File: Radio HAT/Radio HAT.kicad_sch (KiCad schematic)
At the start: 15 parts, among them J1 Raspberry_Pi_2_3, J2 Coax SMA, J3 Barrel_Jack, U1 RFM98PW, U2 AZ2185D-ADJTRG1

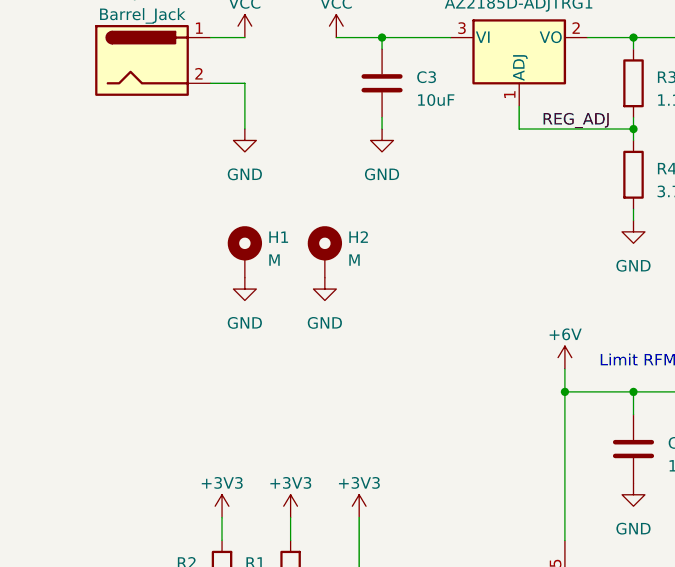
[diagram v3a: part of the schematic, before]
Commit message: Implemented changes from PR
Fixed 3D models of board, added testpoints on board.
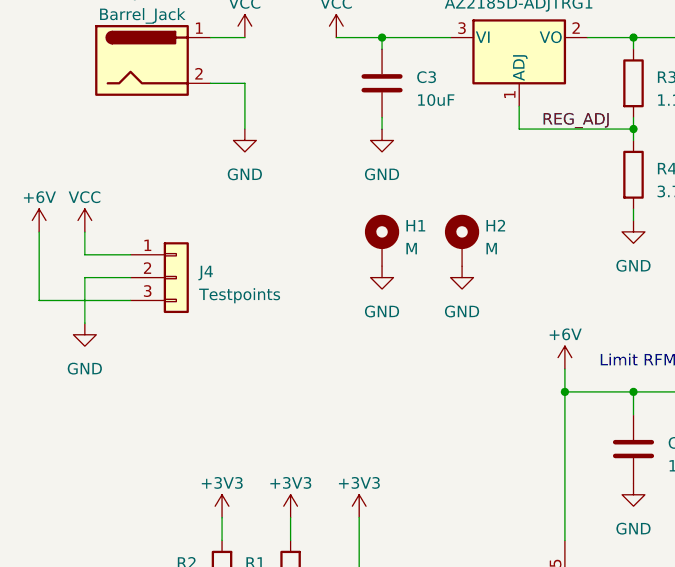
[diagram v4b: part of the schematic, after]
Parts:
- added J4: Testpoints, Connector_PinSocket_2.54mm:PinSocket_1x03_P2.54mm_Vertical, symbol Connector_Generic:Conn_01x03
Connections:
- net +6V: now also J4.3 (Pin_3)
- net GND: now also J4.2 (Pin_2)
- net VCC: now also J4.1 (Pin_1)
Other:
- moved on the sheet: H1, H2
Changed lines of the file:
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@@
+    (stroke (width 0) (type default))
+  )
+  (wire (pts (xy 50.8 80.01) (xy 40.64 80.01))
     (stroke (width 0) (type default))
   )
@@
     (stroke (width 0) (type default))
   )
+  (wire (pts (xy 45.72 72.39) (xy 45.72 74.93))
+    (stroke (width 0) (type default))
+  )
   (wire (pts (xy 63.5 55.88) (xy 63.5 60.96))
     (stroke (width 0) (type default))
@@
     (stroke (width 0) (type default))
   )
+  (wire (pts (xy 45.72 77.47) (xy 50.8 77.47))
+    (stroke (width 0) (type default))
+  )
   (wire (pts (xy 187.96 148.59) (xy 190.5 148.59))
     (stroke (width 0) (type default))
@@
     (stroke (width 0) (type default))
   )
+  (wire (pts (xy 50.8 74.93) (xy 45.72 74.93))
+    (stroke (width 0) (type default))
+  )
   (wire (pts (xy 152.4 109.22) (xy 162.56 109.22))
     (stroke (width 0) (type default))
@@
     (stroke (width 0) (type default))
   )
+  (wire (pts (xy 40.64 80.01) (xy 40.64 72.39))
+    (stroke (width 0) (type default))
+  )
   (wire (pts (xy 99.06 90.17) (xy 99.06 106.68))
     (stroke (width 0) (type default))
@@
   )
   (wire (pts (xy 114.3 121.92) (xy 124.46 121.92))
+    (stroke (width 0) (type default))
+  )
+  (wire (pts (xy 45.72 77.47) (xy 45.72 82.55))
     (stroke (width 0) (type default))
   )
@@
     )
   )
+  (symbol (lib_id "power:VCC") (at 45.72 72.39 0) (unit 1)
+    (in_bom yes) (on_board yes) (dnp no) (fields_autoplaced)
+    (property "Reference" "#PWR020" (at 45.72 76.2 0)
+      (effects (font (size 1.27 1.27)) hide)
+    )
+    (property "Value" "VCC" (at 45.72 68.58 0)
+      (effects (font (size 1.27 1.27)))
+    )
+    (property "Footprint" "" (at 45.72 72.39 0)
+      (effects (font (size 1.27 1.27)) hide)
+    )
+    (property "Datasheet" "" (at 45.72 72.39 0)
+      (effects (font (size 1.27 1.27)) hide)
+    )
+    (pin "1")
+    (instances
+      (project "Radio HAT"
+        (path "/e833ba5c-90ae-4111-9eec-1a872963763a"
+          (reference "#PWR020") (unit 1)
+        )
+      )
+    )
+  )
   (symbol (lib_id "Device:C") (at 78.74 55.88 0) (unit 1)
     (in_bom yes) (on_board yes) (dnp no) (fields_autoplaced)
@@
         (path "/e833ba5c-90ae-4111-9eec-1a872963763a"
           (reference "#PWR03") (unit 1)
+        )
+      )
+    )
+  )
+  (symbol (lib_id "power:GND") (at 45.72 82.55 0) (unit 1)
+    (in_bom yes) (on_board yes) (dnp no)
+    (property "Reference" "#PWR018" (at 45.72 88.9 0)
+      (effects (font (size 1.27 1.27)) hide)
+    )
+    (property "Value" "GND" (at 45.72 87.63 0)
+      (effects (font (size 1.27 1.27)))
+    )
+    (property "Footprint" "" (at 45.72 82.55 0)
+      (effects (font (size 1.27 1.27)) hide)
+    )
+    (property "Datasheet" "" (at 45.72 82.55 0)
+      (effects (font (size 1.27 1.27)) hide)
+    )
+    (pin "1")
+    (instances
+      (project "Radio HAT"
+        (path "/e833ba5c-90ae-4111-9eec-1a872963763a"
+          (reference "#PWR018") (unit 1)
         )
       )
@@
     )
   )
-  (symbol (lib_id "Mechanical:MountingHole_Pad") (at 72.39 74.93 0) (unit 1)
-    (in_bom yes) (on_board yes) (dnp no) (fields_autoplaced)
-    (property "Reference" "H2" (at 74.93 73.025 0)
-      (effects (font (size 1.27 1.27)) (justify left))
-    )
-    (property "Value" "M" (at 74.93 75.565 0)
-      (effects (font (size 1.27 1.27)) (justify left))
-    )
-    (property "Footprint" "MountingHole:MountingHole_2.7mm_M2.5_Pad_Via" (at 72.39 74.93 0)
-      (effects (font (size 1.27 1.27)) hide)
-    )
-    (property "Datasheet" "~" (at 72.39 74.93 0)
+  (symbol (lib_id "Mechanical:MountingHole_Pad") (at 87.63 73.66 0) (unit 1)
+    (in_bom yes) (on_board yes) (dnp no) (fields_autoplaced)
+    (property "Reference" "H2" (at 90.17 71.755 0)
+      (effects (font (size 1.27 1.27)) (justify left))
+    )
+    (property "Value" "M" (at 90.17 74.295 0)
+      (effects (font (size 1.27 1.27)) (justify left))
+    )
+    (property "Footprint" "MountingHole:MountingHole_2.7mm_M2.5_Pad_Via" (at 87.63 73.66 0)
+      (effects (font (size 1.27 1.27)) hide)
+    )
+    (property "Datasheet" "~" (at 87.63 73.66 0)
       (effects (font (size 1.27 1.27)) hide)
     )
@@
     )
   )
-  (symbol (lib_id "Mechanical:MountingHole_Pad") (at 63.5 74.93 0) (unit 1)
-    (in_bom yes) (on_board yes) (dnp no) (fields_autoplaced)
-    (property "Reference" "H1" (at 66.04 73.025 0)
-      (effects (font (size 1.27 1.27)) (justify left))
-    )
-    (property "Value" "M" (at 66.04 75.565 0)
-      (effects (font (size 1.27 1.27)) (justify left))
-    )
-    (property "Footprint" "MountingHole:MountingHole_2.7mm_M2.5_Pad_Via" (at 63.5 74.93 0)
-      (effects (font (size 1.27 1.27)) hide)
-    )
-    (property "Datasheet" "~" (at 63.5 74.93 0)
+  (symbol (lib_id "Mechanical:MountingHole_Pad") (at 78.74 73.66 0) (unit 1)
+    (in_bom yes) (on_board yes) (dnp no) (fields_autoplaced)
+    (property "Reference" "H1" (at 81.28 71.755 0)
+      (effects (font (size 1.27 1.27)) (justify left))
+    )
+    (property "Value" "M" (at 81.28 74.295 0)
+      (effects (font (size 1.27 1.27)) (justify left))
+    )
+    (property "Footprint" "MountingHole:MountingHole_2.7mm_M2.5_Pad_Via" (at 78.74 73.66 0)
+      (effects (font (size 1.27 1.27)) hide)
+    )
+    (property "Datasheet" "~" (at 78.74 73.66 0)
       (effects (font (size 1.27 1.27)) hide)
     )
@@
     )
   )
+  (symbol (lib_id "power:+6V") (at 40.64 72.39 0) (unit 1)
+    (in_bom yes) (on_board yes) (dnp no) (fields_autoplaced)
+    (property "Reference" "#PWR021" (at 40.64 76.2 0)
+      (effects (font (size 1.27 1.27)) hide)
+    )
+    (property "Value" "+6V" (at 40.64 68.58 0)
+      (effects (font (size 1.27 1.27)))
+    )
+    (property "Footprint" "" (at 40.64 72.39 0)
+      (effects (font (size 1.27 1.27)) hide)
+    )
+    (property "Datasheet" "" (at 40.64 72.39 0)
+      (effects (font (size 1.27 1.27)) hide)
+    )
+    (pin "1")
+    (instances
+      (project "Radio HAT"
+        (path "/e833ba5c-90ae-4111-9eec-1a872963763a"
+          (reference "#PWR021") (unit 1)
+        )
+      )
+    )
+  )
   (symbol (lib_id "Connector:Barrel_Jack") (at 52.07 53.34 0) (unit 1)
     (in_bom yes) (on_board yes) (dnp no) (fields_autoplaced)
@@
     )
   )
-  (symbol (lib_id "power:GND") (at 63.5 77.47 0) (unit 1)
-    (in_bom yes) (on_board yes) (dnp no)
-    (property "Reference" "#PWR016" (at 63.5 83.82 0)
-      (effects (font (size 1.27 1.27)) hide)
-    )
-    (property "Value" "GND" (at 63.5 82.55 0)
-      (effects (font (size 1.27 1.27)))
-    )
-    (property "Footprint" "" (at 63.5 77.47 0)
-      (effects (font (size 1.27 1.27)) hide)
-    )
-    (property "Datasheet" "" (at 63.5 77.47 0)
+  (symbol (lib_id "power:GND") (at 78.74 76.2 0) (unit 1)
+    (in_bom yes) (on_board yes) (dnp no)
+    (property "Reference" "#PWR016" (at 78.74 82.55 0)
+      (effects (font (size 1.27 1.27)) hide)
+    )
+    (property "Value" "GND" (at 78.74 81.28 0)
+      (effects (font (size 1.27 1.27)))
+    )
+    (property "Footprint" "" (at 78.74 76.2 0)
+      (effects (font (size 1.27 1.27)) hide)
+    )
+    (property "Datasheet" "" (at 78.74 76.2 0)
       (effects (font (size 1.27 1.27)) hide)
     )
@@
         (path "/e833ba5c-90ae-4111-9eec-1a872963763a"
           (reference "#PWR016") (unit 1)
+        )
+      )
+    )
+  )
+  (symbol (lib_id "Connector_Generic:Conn_01x03") (at 55.88 77.47 0) (unit 1)
+    (in_bom yes) (on_board yes) (dnp no) (fields_autoplaced)
+    (property "Reference" "J4" (at 58.42 76.835 0)
+      (effects (font (size 1.27 1.27)) (justify left))
+    )
+    (property "Value" "Testpoints" (at 58.42 79.375 0)
+      (effects (font (size 1.27 1.27)) (justify left))
+    )
+    (property "Footprint" "Connector_PinSocket_2.54mm:PinSocket_1x03_P2.54mm_Vertical" (at 55.88 77.47 0)
+      (effects (font (size 1.27 1.27)) hide)
+    )
+    (property "Datasheet" "~" (at 55.88 77.47 0)
+      (effects (font (size 1.27 1.27)) hide)
+    )
+    (pin "1")
+    (pin "2")
+    (pin "3")
+    (instances
+      (project "Radio HAT"
+        (path "/e833ba5c-90ae-4111-9eec-1a872963763a"
+          (reference "J4") (unit 1)
         )
       )
@@
     )
   )
-  (symbol (lib_id "power:GND") (at 72.39 77.47 0) (unit 1)
-    (in_bom yes) (on_board yes) (dnp no)
-    (property "Reference" "#PWR019" (at 72.39 83.82 0)
-      (effects (font (size 1.27 1.27)) hide)
-    )
-    (property "Value" "GND" (at 72.39 82.55 0)
-      (effects (font (size 1.27 1.27)))
-    )
-    (property "Footprint" "" (at 72.39 77.47 0)
-      (effects (font (size 1.27 1.27)) hide)
-    )
-    (property "Datasheet" "" (at 72.39 77.47 0)
-      (effects (font (size 1.27 1.27)) hide)
-    )
+  (symbol (lib_id "power:GND") (at 87.63 76.2 0) (unit 1)
+    (in_bom yes) (on_board yes) (dnp no)
+    (property "Reference" "#PWR019" (at 87.63 82.55 0)
+      (effects (font (size 1.27 1.27)) hide)
+    )
+    (property "Value" "GND" (at 87.63 81.28 0)
+      (effects (font (size 1.27 1.27)))
+    )
+    (property "Footprint" "" (at 87.63 76.2 0)
+      (effects (font (size 1.27 1.27)) hide)
+    )
+    (property "Datasheet" "" (at 87.63 76.2 0)
+      (effects (font (size 1.27 1.27)) hide)
+    )

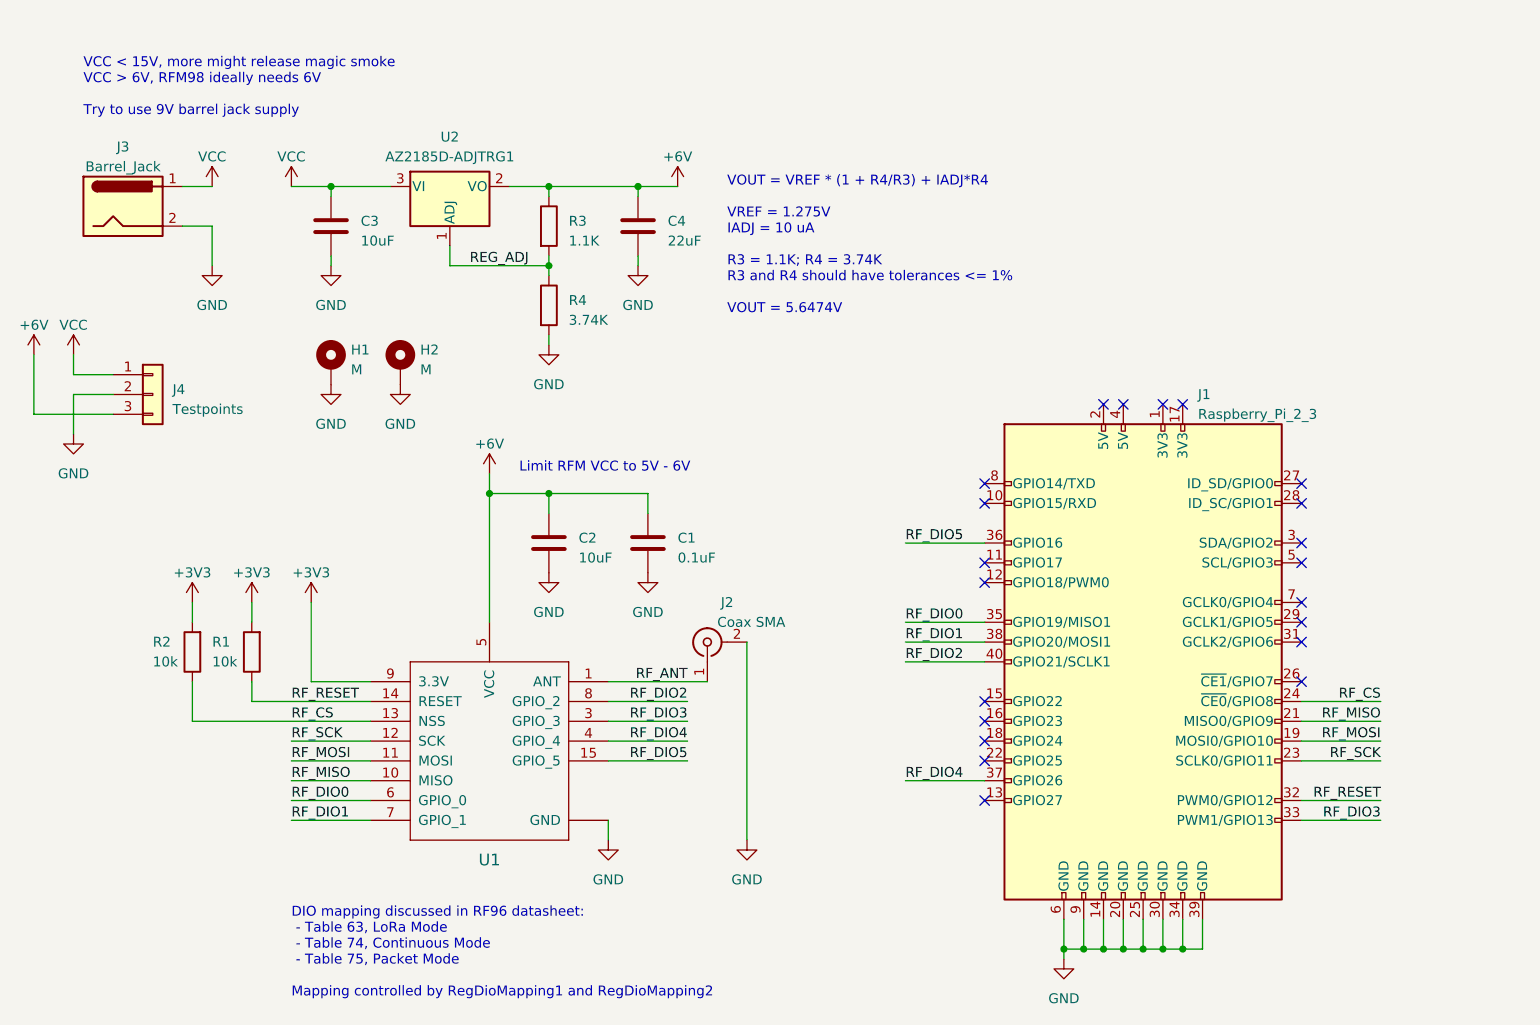
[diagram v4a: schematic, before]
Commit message: Changed connector orientation
Changed orientation of 40-pin connector, increased board size, added optional pot, added graphics
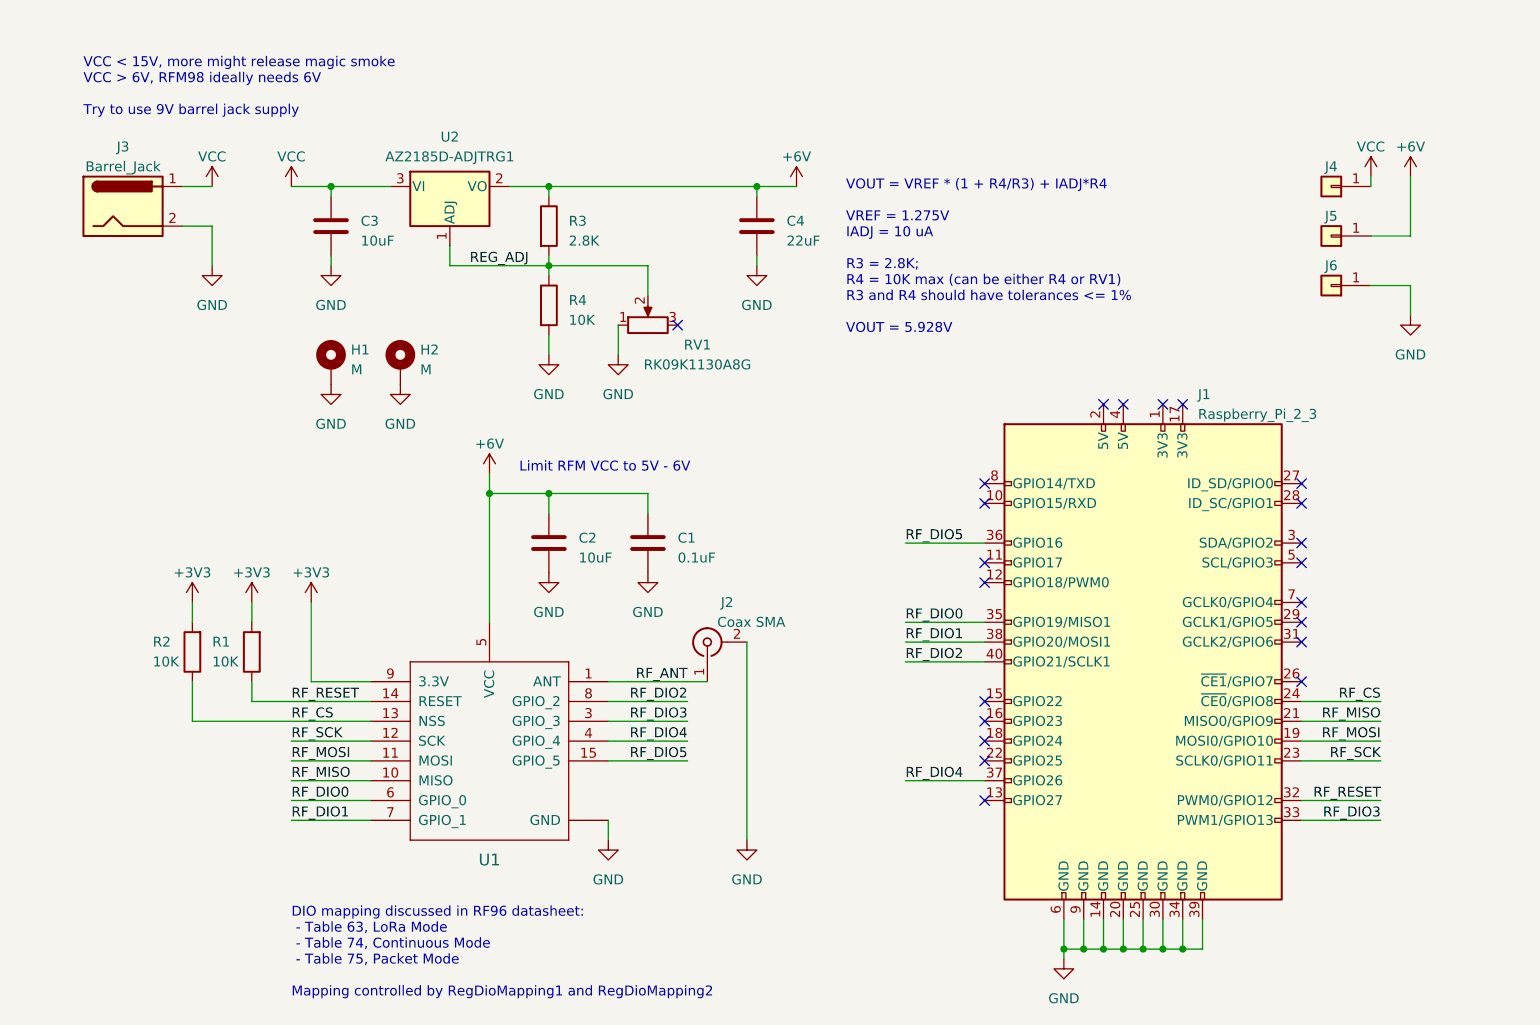
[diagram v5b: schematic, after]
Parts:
- removed J4: Testpoints, Connector_PinSocket_2.54mm:PinSocket_1x03_P2.54mm_Vertical, symbol Connector_Generic:Conn_01x03
- added J4: VCC, TestPoint:TestPoint_Loop_D2.50mm_Drill1.0mm, symbol Connector_Generic:Conn_01x01
- added J5: 6V, TestPoint:TestPoint_Loop_D2.50mm_Drill1.0mm, symbol Connector_Generic:Conn_01x01
- added J6: GND, TestPoint:TestPoint_Loop_D2.50mm_Drill1.0mm, symbol Connector_Generic:Conn_01x01
- added RV1: RK09K1130A8G, Potentiometer_THT:Potentiometer_Alps_RK09K_Single_Vertical, symbol Device:R_Potentiometer
- R1, R2: value 10k -> 10K
- R3: value 1.1K -> 2.8K
- R4: value 3.74K -> 10K
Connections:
- net +6V: now also J5.1 (Pin_1)
- net GND: now also J6.1 (Pin_1), RV1.1
- net REG_ADJ: now also RV1.2
- net VCC: now also J4.1 (Pin_1)
- no-connect marks 21 -> 22
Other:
- note added: "VOUT = VREF * (1 + R4/R3) + IADJ*R4 VREF = 1.275V IADJ = 10 uA R3 = 2.8K; R4 = 10K max (can be either R4 or RV1) R3 and R4 should have tolerances <= 1% VOUT = 5.928V"
- note removed: "VOUT = VREF * (1 + R4/R3) + IADJ*R4 VREF = 1.275V IADJ = 10 uA R3 = 1.1K; R4 = 3.74K R3 and R4 should have tolerances <= 1% VOUT = 5.6474V"
- company: Carnegie Mellon University -> LICENSE: CC BY 4.0
- moved on the sheet: C4

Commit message: Implemented PR feedback by Jason
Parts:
- added R5: 0, Resistor_SMD:R_1206_3216Metric_Pad1.30x1.75mm_HandSolder, symbol Device:R
- added R6: 0, Resistor_SMD:R_0805_2012Metric_Pad1.20x1.40mm_HandSolder, symbol Device:R
- C1, C2: footprint Capacitor_SMD:C_0805_2012Metric_Pad1.18x1.45mm_HandSolder -> Capacitor_SMD:C_0603_1608Metric_Pad1.08x0.95mm_HandSolder
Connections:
- net +6V: now also R5.1; no longer C1.1, C2.1, U1.5 (VCC)
- net REG_ADJ: now also R6.1; no longer RV1.2
- new net: R6.2, RV1.2
- new net V_RF: C1.1, C2.1, R5.2, U1.5 (VCC)
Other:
- note added: "C3 needs to be rated for AT LEAST 10V"
- moved on the sheet: C4, R3, R4, RV1
